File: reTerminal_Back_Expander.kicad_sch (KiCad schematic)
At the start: 1 part

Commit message: Add FX23 footprint
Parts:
- J1: renamed from J?; footprint (none) -> local:FX23-100S
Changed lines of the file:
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@@
   (symbol (lib_id "power:PWR_FLAG") (at 194.31 25.4 0) (unit 1)
     (in_bom yes) (on_board yes) (fields_autoplaced)
-    (property "Reference" "#FLG?" (id 0) (at 194.31 23.495 0)
+    (property "Reference" "#FLG0101" (id 0) (at 194.31 23.495 0)
       (effects (font (size 1.27 1.27)) hide)
     )
@@
   (symbol (lib_id "power:GND") (at 207.01 25.4 0) (unit 1)
     (in_bom yes) (on_board yes) (fields_autoplaced)
-    (property "Reference" "#PWR?" (id 0) (at 207.01 31.75 0)
+    (property "Reference" "#PWR0103" (id 0) (at 207.01 31.75 0)
       (effects (font (size 1.27 1.27)) hide)
     )
@@
   (symbol (lib_id "power:+3.3V") (at 114.3 29.21 0) (unit 1)
     (in_bom yes) (on_board yes) (fields_autoplaced)
-    (property "Reference" "#PWR?" (id 0) (at 114.3 33.02 0)
+    (property "Reference" "#PWR0106" (id 0) (at 114.3 33.02 0)
       (effects (font (size 1.27 1.27)) hide)
     )
@@
   (symbol (lib_id "power:GND") (at 212.09 25.4 0) (unit 1)
     (in_bom yes) (on_board yes) (fields_autoplaced)
-    (property "Reference" "#PWR?" (id 0) (at 212.09 31.75 0)
+    (property "Reference" "#PWR0104" (id 0) (at 212.09 31.75 0)
       (effects (font (size 1.27 1.27)) hide)
     )
@@
   (symbol (lib_id "power:GND") (at 88.9 171.45 0) (unit 1)
     (in_bom yes) (on_board yes) (fields_autoplaced)
-    (property "Reference" "#PWR?" (id 0) (at 88.9 177.8 0)
+    (property "Reference" "#PWR0109" (id 0) (at 88.9 177.8 0)
       (effects (font (size 1.27 1.27)) hide)
     )
@@
   (symbol (lib_id "power:GND") (at 132.08 171.45 0) (unit 1)
     (in_bom yes) (on_board yes)
-    (property "Reference" "#PWR?" (id 0) (at 132.08 177.8 0)
+    (property "Reference" "#PWR0108" (id 0) (at 132.08 177.8 0)
       (effects (font (size 1.27 1.27)) hide)
     )
@@
   (symbol (lib_id "power:+3.3V") (at 207.01 25.4 0) (unit 1)
     (in_bom yes) (on_board yes) (fields_autoplaced)
-    (property "Reference" "#PWR?" (id 0) (at 207.01 29.21 0)
+    (property "Reference" "#PWR0101" (id 0) (at 207.01 29.21 0)
       (effects (font (size 1.27 1.27)) hide)
     )
@@
   (symbol (lib_id "power:+5V") (at 212.09 25.4 0) (unit 1)
     (in_bom yes) (on_board yes)
-    (property "Reference" "#PWR?" (id 0) (at 212.09 29.21 0)
+    (property "Reference" "#PWR0105" (id 0) (at 212.09 29.21 0)
       (effects (font (size 1.27 1.27)) hide)
     )
@@
   (symbol (lib_id "power:+5V") (at 107.95 179.07 180) (unit 1)
     (in_bom yes) (on_board yes)
-    (property "Reference" "#PWR?" (id 0) (at 107.95 175.26 0)
+    (property "Reference" "#PWR0110" (id 0) (at 107.95 175.26 0)
       (effects (font (size 1.27 1.27)) hide)
     )
@@
   (symbol (lib_id "power:+3.3V") (at 106.68 29.21 0) (unit 1)
     (in_bom yes) (on_board yes) (fields_autoplaced)
-    (property "Reference" "#PWR?" (id 0) (at 106.68 33.02 0)
+    (property "Reference" "#PWR0107" (id 0) (at 106.68 33.02 0)
       (effects (font (size 1.27 1.27)) hide)
     )
@@
   (symbol (lib_id "power:+5V") (at 113.03 179.07 180) (unit 1)
     (in_bom yes) (on_board yes)
-    (property "Reference" "#PWR?" (id 0) (at 113.03 175.26 0)
+    (property "Reference" "#PWR0111" (id 0) (at 113.03 175.26 0)
       (effects (font (size 1.27 1.27)) hide)
     )
@@
   (symbol (lib_id "power:GND") (at 194.31 25.4 0) (unit 1)
     (in_bom yes) (on_board yes) (fields_autoplaced)
-    (property "Reference" "#PWR?" (id 0) (at 194.31 31.75 0)
+    (property "Reference" "#PWR0102" (id 0) (at 194.31 31.75 0)
       (effects (font (size 1.27 1.27)) hide)
     )
@@
   (symbol (lib_id "local:Hirose-FX23-100-reTerminal") (at 110.49 104.14 0) (unit 1)
     (in_bom yes) (on_board yes)
-    (property "Reference" "J?" (id 0) (at 115.57 33.02 0)
+    (property "Reference" "J1" (id 0) (at 115.57 33.02 0)
       (effects (font (size 1.27 1.27)) (justify left))
     )
@@
       (effects (font (size 1.27 1.27)) (justify left))
     )
-    (property "Footprint" "" (id 2) (at 110.49 22.86 0)
+    (property "Footprint" "local:FX23-100S" (id 2) (at 110.49 22.86 0)
       (effects (font (size 1.27 1.27)) hide)
     )
@@
   (symbol_instances
     (path "/01ccc412-83ac-4f51-aa4c-3b661b9cc31f"
-      (reference "#FLG?") (unit 1) (value "PWR_FLAG") (footprint "")
+      (reference "#FLG0101") (unit 1) (value "PWR_FLAG") (footprint "")
+    )
+    (path "/74f8fddb-6258-44e8-b90f-80c7c2ee9d8d"
+      (reference "#PWR0101") (unit 1) (value "+3.3V") (footprint "")
+    )
+    (path "/e22c9d7c-a4ad-470a-9ae4-c471bc4ed5b3"
+      (reference "#PWR0102") (unit 1) (value "GND") (footprint "")
     )
     (path "/2538d8da-0be0-4cb6-85e3-45ef00e92339"
-      (reference "#PWR?") (unit 1) (value "GND") (footprint "")
+      (reference "#PWR0103") (unit 1) (value "GND") (footprint "")
+    )
+    (path "/3440db19-ae34-4c34-a41c-c85957effa98"
+      (reference "#PWR0104") (unit 1) (value "GND") (footprint "")
+    )
+    (path "/8ad53537-f344-4246-88ee-167f9a1f169a"
+      (reference "#PWR0105") (unit 1) (value "+5V") (footprint "")
     )
     (path "/2c14381d-3290-4c1f-a7d4-9d3af132b225"
-      (reference "#PWR?") (unit 1) (value "+3.3V") (footprint "")
-    )
-    (path "/3440db19-ae34-4c34-a41c-c85957effa98"
-      (reference "#PWR?") (unit 1) (value "GND") (footprint "")
+      (reference "#PWR0106") (unit 1) (value "+3.3V") (footprint "")
+    )
+    (path "/a15e78be-a618-49bd-8e26-50eba3fc88d5"
+      (reference "#PWR0107") (unit 1) (value "+3.3V") (footprint "")
+    )
+    (path "/66df8548-fddc-480f-ac16-94c0896245ab"
+      (reference "#PWR0108") (unit 1) (value "GND") (footprint "")
     )
     (path "/502a5913-ee24-401f-9f1a-9d3a372ca6ac"
-      (reference "#PWR?") (unit 1) (value "GND") (footprint "")
-    )
-    (path "/66df8548-fddc-480f-ac16-94c0896245ab"
-      (reference "#PWR?") (unit 1) (value "GND") (footprint "")
-    )
-    (path "/74f8fddb-6258-44e8-b90f-80c7c2ee9d8d"
-      (reference "#PWR?") (unit 1) (value "+3.3V") (footprint "")
-    )
-    (path "/8ad53537-f344-4246-88ee-167f9a1f169a"
-      (reference "#PWR?") (unit 1) (value "+5V") (footprint "")
+      (reference "#PWR0109") (unit 1) (value "GND") (footprint "")
     )
     (path "/90dee011-b0ad-43a3-a8fb-2468a2662b76"
-      (reference "#PWR?") (unit 1) (value "+5V") (footprint "")
-    )
-    (path "/a15e78be-a618-49bd-8e26-50eba3fc88d5"
-      (reference "#PWR?") (unit 1) (value "+3.3V") (footprint "")
+      (reference "#PWR0110") (unit 1) (value "+5V") (footprint "")
     )
     (path "/df222b17-6b29-4037-b5ed-8146a025d802"
-      (reference "#PWR?") (unit 1) (value "+5V") (footprint "")
-    )
-    (path "/e22c9d7c-a4ad-470a-9ae4-c471bc4ed5b3"
-      (reference "#PWR?") (unit 1) (value "GND") (footprint "")
+      (reference "#PWR0111") (unit 1) (value "+5V") (footprint "")
     )
     (path "/eb143dfe-15bd-42d2-b83f-23b8ef19dd74"
-      (reference "J?") (unit 1) (value "Hirose-FX23-100-reTerminal") (footprint "")
-    )
-  )
+      (reference "J1") (unit 1) (value "Hirose-FX23-100-reTerminal") (footprint "local:FX23-100S")
+    )
+  )

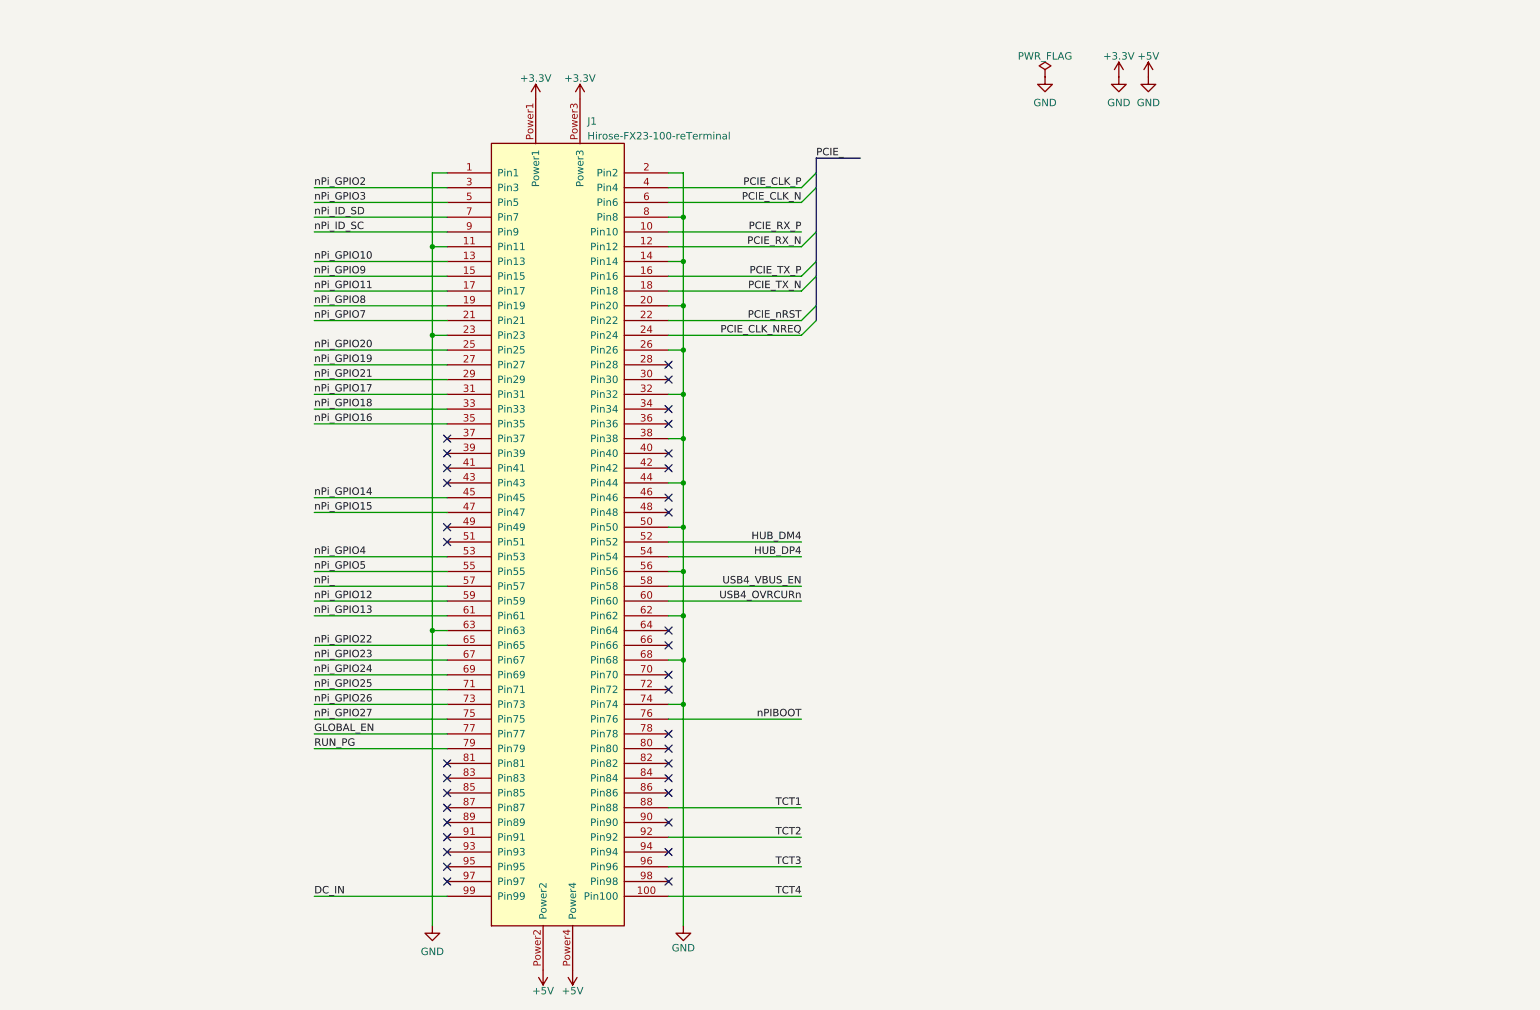
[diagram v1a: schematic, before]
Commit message: Add M.2 connector
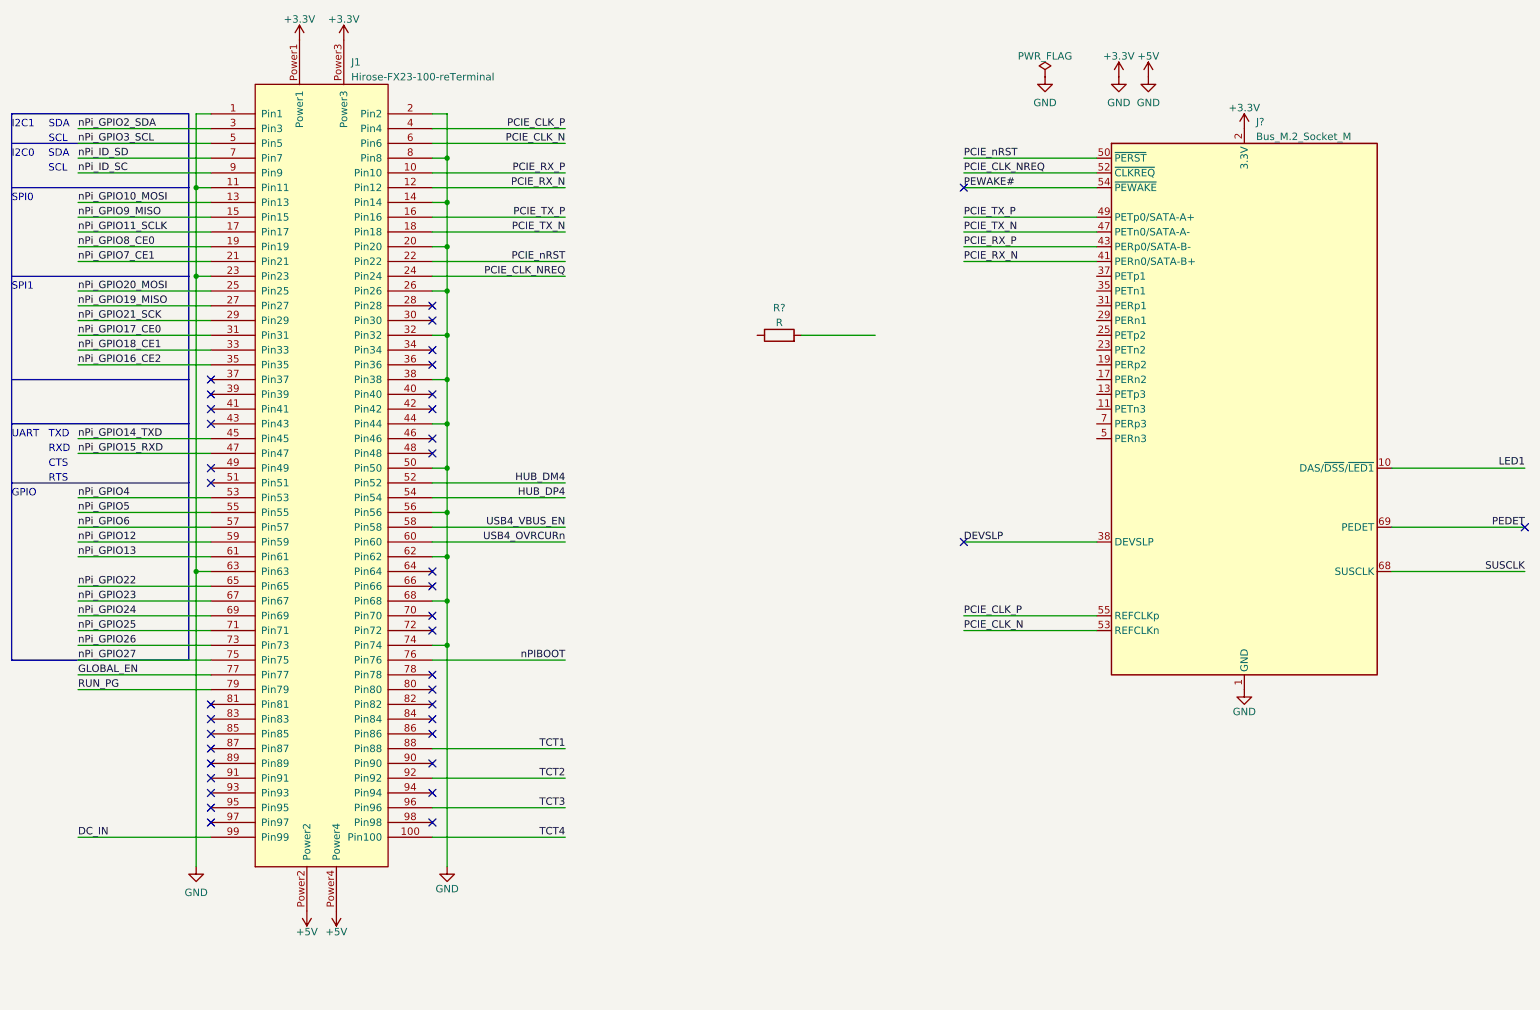
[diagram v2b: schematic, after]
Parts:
- added J?: Bus_M.2_Socket_M, symbol Connector:Bus_M.2_Socket_M
- added R?: R, Resistor_SMD:R_0402_1005Metric, symbol Device:R
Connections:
- net +3V3: now also J?.1 (GND), J?.12 (3.3V), J?.14 (3.3V), J?.15 (GND), J?.16 (3.3V), J?.18 (3.3V), J?.2 (3.3V), J?.21 (GND), J?.27 (GND), J?.3 (GND), J?.33 (GND), J?.39 (GND), J?.4 (3.3V), J?.45 (GND), J?.51 (GND), J?.57 (GND), J?.70 (3.3V), J?.71 (GND), J?.72 (3.3V), J?.73 (GND), J?.74 (3.3V), J?.75 (GND), J?.9 (GND)
- net PCIE_CLK_N: now also J?.53 (REFCLKn)
- net PCIE_CLK_NREQ: now also J?.52 (~{CLKREQ})
- net PCIE_CLK_P: now also J?.55 (REFCLKp)
- net PCIE_RX_N: now also J?.41 (PERn0/SATA-B+)
- net PCIE_RX_P: now also J?.43 (PERp0/SATA-B-)
- net PCIE_TX_N: now also J?.47 (PETn0/SATA-A-)
- net PCIE_TX_P: now also J?.49 (PETp0/SATA-A+)
- net PCIE_nRST: now also J?.50 (~{PERST})
- net nPi_ renamed nPi_GPIO6
- net nPi_GPIO10 renamed nPi_GPIO10_MOSI
- net nPi_GPIO11 renamed nPi_GPIO11_SCLK
- net nPi_GPIO14 renamed nPi_GPIO14_TXD
- net nPi_GPIO15 renamed nPi_GPIO15_RXD
- net nPi_GPIO16 renamed nPi_GPIO16_CE2
- net nPi_GPIO17 renamed nPi_GPIO17_CE0
- net nPi_GPIO18 renamed nPi_GPIO18_CE1
- net nPi_GPIO19 renamed nPi_GPIO19_MISO
- net nPi_GPIO2 renamed nPi_GPIO2_SDA
- net nPi_GPIO20 renamed nPi_GPIO20_MOSI
- net nPi_GPIO21 renamed nPi_GPIO21_SCK
- net nPi_GPIO3 renamed nPi_GPIO3_SCL
- net nPi_GPIO7 renamed nPi_GPIO7_CE1
- net nPi_GPIO8 renamed nPi_GPIO8_CE0
- net nPi_GPIO9 renamed nPi_GPIO9_MISO
- new net DEVSLP: J?.38 (DEVSLP)
- new net PEDET: J?.69 (PEDET)
- new net PEWAKE#: J?.54 (~{PEWAKE})
- new net SUSCLK: J?.68 (SUSCLK)
- no-connect marks 35 -> 38
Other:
- note added: "CTS"
- note added: "GPIO"
- note added: "I2C0"
- note added: "I2C1"
- note added: "RTS"
- note added: "RXD"
- note added: "SCL"
- note added: "SDA"
- note added: "SPI0"
- note added: "SPI1"
- note added: "TXD"
- note added: "UART"
- moved on the sheet: J1
